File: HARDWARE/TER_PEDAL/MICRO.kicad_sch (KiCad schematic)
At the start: 21 parts, among them SW1 RST, U1 STM32F103C8Tx, Y1 8mHz

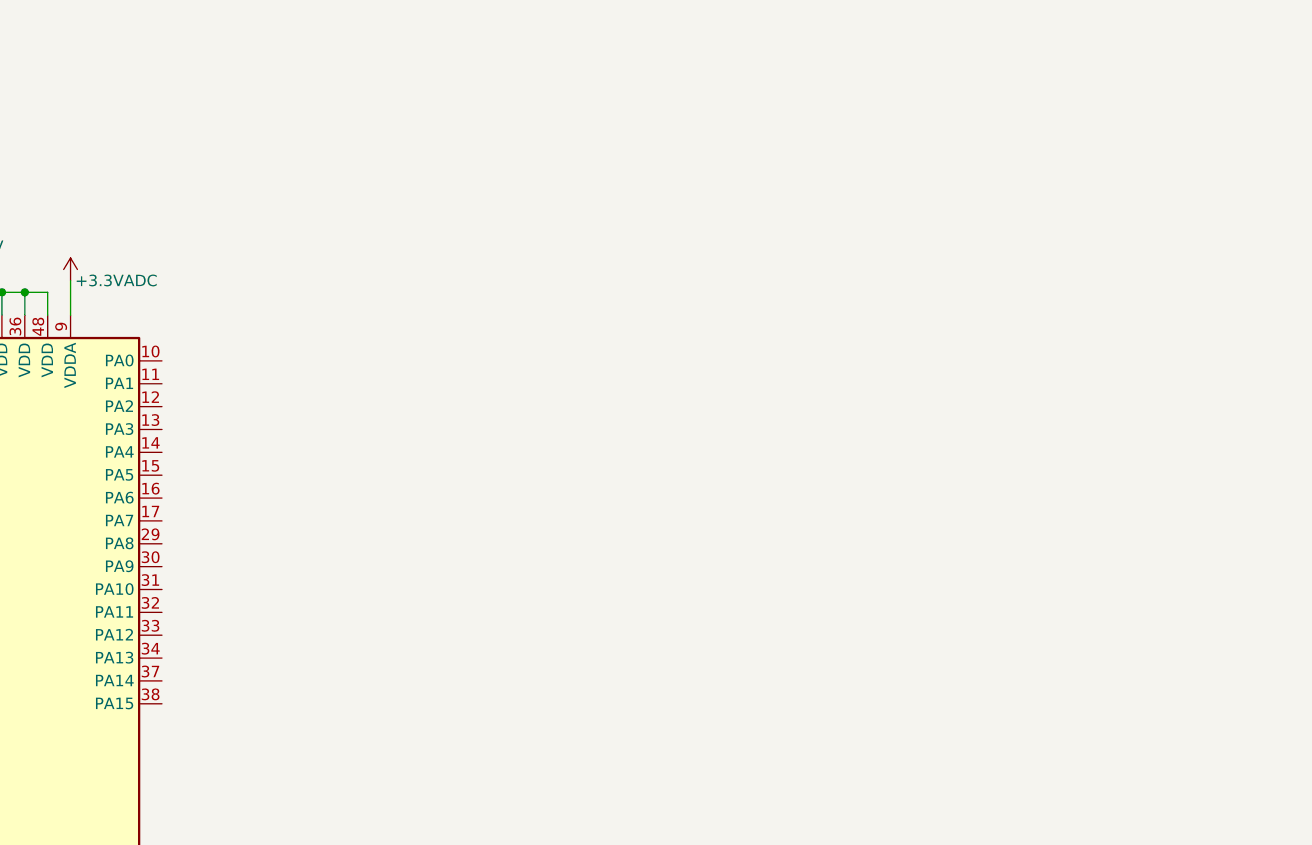
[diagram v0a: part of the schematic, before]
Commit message: Added Uniport, Debug and began sensors design
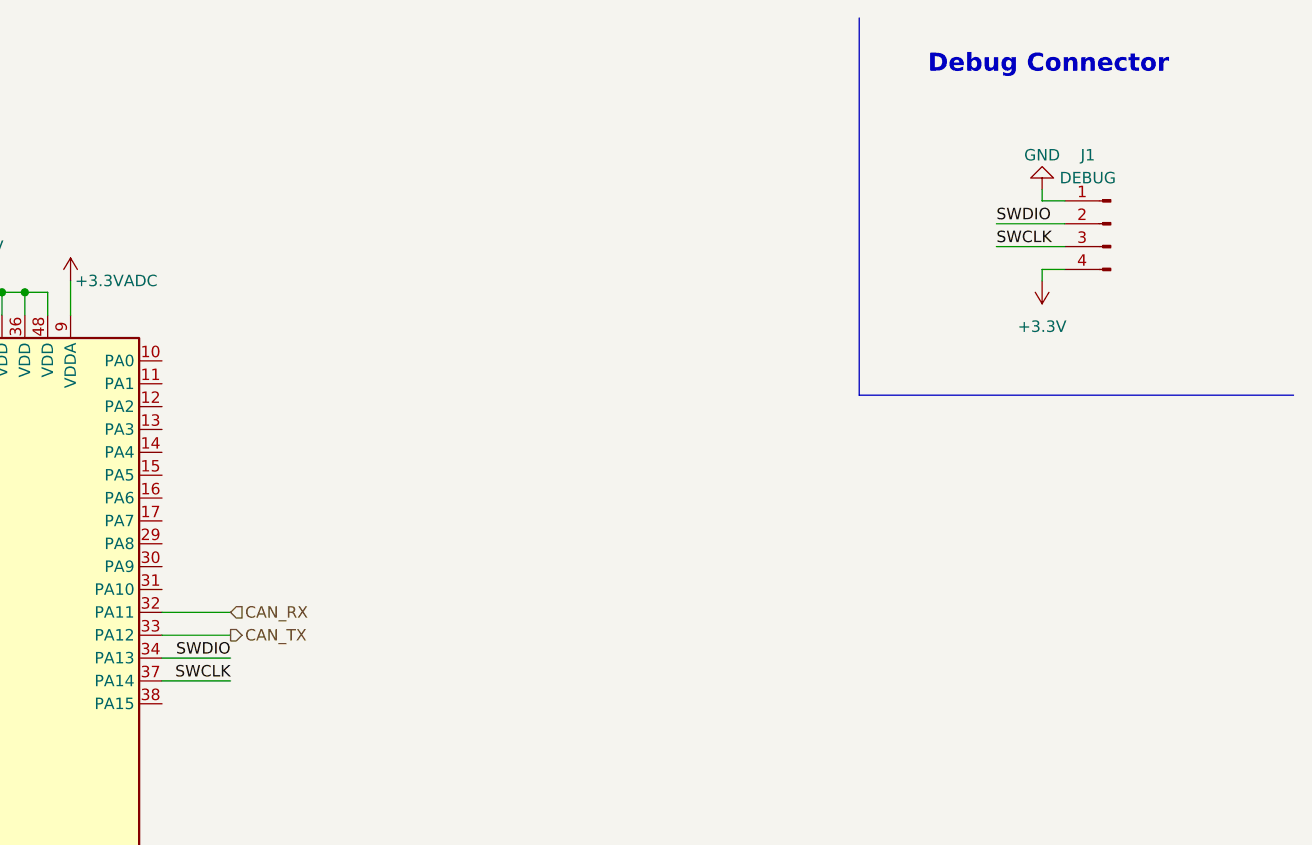
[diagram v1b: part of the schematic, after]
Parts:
- added J1: DEBUG, symbol Connector:Conn_01x04_Male
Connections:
- net GND: now also J1.1 (Pin_1)
- net CAN_RX: now reaches U1.32 (PA11)
- net CAN_TX: now reaches U1.33 (PA12)
- net SWDIO: now reaches U1.34 (PA13)
- net SWDIO: now also J1.2 (Pin_2)
- net SWCLK: now reaches U1.37 (PA14)
- net SWCLK: now also J1.3 (Pin_3)
- new net +3V3: J1.4 (Pin_4)
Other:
- note added: "Debug Connector"
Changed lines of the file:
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@@
+    (stroke (width 0) (type default))
+  )
+  (wire (pts (xy 158.75 83.82) (xy 166.37 83.82))
+    (stroke (width 0) (type default))
+  )
+  (wire (pts (xy 256.54 40.64) (xy 256.54 41.91))
     (stroke (width 0) (type default))
   )
@@
     (stroke (width 0) (type default))
   )
+  (wire (pts (xy 251.46 35.56) (xy 259.08 35.56))
+    (stroke (width 0) (type default))
+  )
   (wire (pts (xy 36.83 157.48) (xy 38.1 157.48))
     (stroke (width 0) (type default))
@@
     (stroke (width 0) (type default))
   )
+  (wire (pts (xy 256.54 31.75) (xy 256.54 33.02))
+    (stroke (width 0) (type default))
+  )
   (wire (pts (xy 138.43 41.91) (xy 138.43 43.18))
     (stroke (width 0) (type default))
@@
     (stroke (width 0) (type default))
   )
+  (wire (pts (xy 251.46 38.1) (xy 259.08 38.1))
+    (stroke (width 0) (type default))
+  )
   (wire (pts (xy 118.11 83.82) (xy 125.73 83.82))
     (stroke (width 0) (type default))
@@
     (stroke (width 0) (type default))
   )
+  (wire (pts (xy 158.75 86.36) (xy 166.37 86.36))
+    (stroke (width 0) (type default))
+  )
   (wire (pts (xy 148.59 41.91) (xy 148.59 45.72))
     (stroke (width 0) (type default))
@@
     (stroke (width 0) (type default))
   )
+  (polyline (pts (xy 236.22 54.61) (xy 284.48 54.61))
+    (stroke (width 0) (type default))
+  )
+  (polyline (pts (xy 236.22 12.7) (xy 236.22 54.61))
+    (stroke (width 0) (type default))
+  )
   (wire (pts (xy 143.51 43.18) (xy 146.05 43.18))
     (stroke (width 0) (type default))
@@
     (stroke (width 0) (type default))
   )
+  (wire (pts (xy 256.54 33.02) (xy 259.08 33.02))
+    (stroke (width 0) (type default))
+  )
   (wire (pts (xy 36.83 154.94) (xy 36.83 157.48))
     (stroke (width 0) (type default))
@@
     (stroke (width 0) (type default))
   )
+  (wire (pts (xy 158.75 78.74) (xy 166.37 78.74))
+    (stroke (width 0) (type default))
+  )
+  (wire (pts (xy 158.75 81.28) (xy 166.37 81.28))
+    (stroke (width 0) (type default))
+  )
   (wire (pts (xy 40.64 115.57) (xy 40.64 116.84))
     (stroke (width 0) (type default))
@@
   )
   (wire (pts (xy 24.13 115.57) (xy 24.13 116.84))
+    (stroke (width 0) (type default))
+  )
+  (wire (pts (xy 259.08 40.64) (xy 256.54 40.64))
     (stroke (width 0) (type default))
   )
@@
     (effects (font (size 1.27 1.27)) (justify left bottom))
   )
+  (text "Debug Connector" (at 243.84 19.05 0)
+    (effects (font (size 2 2) (thickness 0.4) bold) (justify left bottom))
+  )
+  (label "SWCLK" (at 251.46 38.1 0) (fields_autoplaced)
+    (effects (font (size 1.27 1.27)) (justify left bottom))
+  )
+  (label "SWCLK" (at 166.37 86.36 180) (fields_autoplaced)
+    (effects (font (size 1.27 1.27)) (justify right bottom))
+  )
+  (label "SWDIO" (at 251.46 35.56 0) (fields_autoplaced)
+    (effects (font (size 1.27 1.27)) (justify left bottom))
+  )
   (label "BOOT1" (at 118.11 83.82 0) (fields_autoplaced)
     (effects (font (size 1.27 1.27)) (justify left bottom))
@@
     (effects (font (size 1.27 1.27)) (justify left bottom))
   )
+  (label "SWDIO" (at 166.37 83.82 180) (fields_autoplaced)
+    (effects (font (size 1.27 1.27)) (justify right bottom))
+  )
   (label "NRST" (at 118.11 50.8 0) (fields_autoplaced)
     (effects (font (size 1.27 1.27)) (justify left bottom))
@@
   (label "BOOT1" (at 48.26 125.73 180) (fields_autoplaced)
     (effects (font (size 1.27 1.27)) (justify right bottom))
+  )
+  (hierarchical_label "CAN_RX" (shape input) (at 166.37 78.74 0) (fields_autoplaced)
+    (effects (font (size 1.27 1.27)) (justify left))
+  )
+  (hierarchical_label "CAN_TX" (shape output) (at 166.37 81.28 0) (fields_autoplaced)
+    (effects (font (size 1.27 1.27)) (justify left))
   )
   (symbol (lib_id "Device:C") (at 16.51 55.88 0) (unit 1)
@@
         (path "/73ede3a3-6344-40fe-9207-10ff50d388ba/7632a94a-0691-4527-83e2-6d814eae7e64"
           (reference "C1") (unit 1)
+        )
+      )
+    )
+  )
+  (symbol (lib_id "Connector:Conn_01x04_Male") (at 264.16 35.56 0) (mirror y) (unit 1)
+    (in_bom yes) (on_board yes) (dnp no)
+    (property "Reference" "J1" (at 261.62 27.94 0)
+      (effects (font (size 1.27 1.27)))
+    )
+    (property "Value" "DEBUG" (at 261.62 30.48 0)
+      (effects (font (size 1.27 1.27)))
+    )
+    (property "Footprint" "" (at 264.16 35.56 0)
+      (effects (font (size 1.27 1.27)) hide)
+    )
+    (property "Datasheet" "~" (at 264.16 35.56 0)
+      (effects (font (size 1.27 1.27)) hide)
+    )
+    (pin "1")
+    (pin "2")
+    (pin "3")
+    (pin "4")
+    (instances
+      (project "TER_PEDAL"
+        (path "/73ede3a3-6344-40fe-9207-10ff50d388ba/7632a94a-0691-4527-83e2-6d814eae7e64"
+          (reference "J1") (unit 1)
         )
       )
@@
     )
   )
+  (symbol (lib_name "GND_1") (lib_id "power:GND") (at 256.54 31.75 180) (unit 1)
+    (in_bom yes) (on_board yes) (dnp no) (fields_autoplaced)
+    (property "Reference" "#PWR032" (at 256.54 25.4 0)
+      (effects (font (size 1.27 1.27)) hide)
+    )
+    (property "Value" "GND" (at 256.54 27.94 0)
+      (effects (font (size 1.27 1.27)))
+    )
+    (property "Footprint" "" (at 256.54 31.75 0)
+      (effects (font (size 1.27 1.27)) hide)
+    )
+    (property "Datasheet" "" (at 256.54 31.75 0)
+      (effects (font (size 1.27 1.27)) hide)
+    )
+    (pin "1")
+    (instances
+      (project "TER_PEDAL"
+        (path "/73ede3a3-6344-40fe-9207-10ff50d388ba/7632a94a-0691-4527-83e2-6d814eae7e64"
+          (reference "#PWR032") (unit 1)
+        )
+      )
+    )
+  )
   (symbol (lib_id "Device:C_Small") (at 22.86 27.94 0) (unit 1)
     (in_bom yes) (on_board yes) (dnp no)
@@
         )
       )
+    )
+  )
+  (symbol (lib_name "+3.3V_1") (lib_id "power:+3.3V") (at 256.54 41.91 180) (unit 1)
+    (in_bom yes) (on_board yes) (dnp no) (fields_autoplaced)
+    (property "Reference" "#PWR033" (at 256.54 38.1 0)
+      (effects (font (size 1.27 1.27)) hide)
+    )
+    (property "Value" "+3.3V" (at 256.54 46.99 0)
+      (effects (font (size 1.27 1.27)))
+    )
+    (property "Footprint" "" (at 256.54 41.91 0)
+      (effects (font (size 1.27 1.27)) hide)
+    )
+    (property "Datasheet" "" (at 256.54 41.91 0)
+      (effects (font (size 1.27 1.27)) hide)
+    )
+    (pin "1")
+    (instances
+      (project "TER_PEDAL"
+        (path "/73ede3a3-6344-40fe-9207-10ff50d388ba/7632a94a-0691-4527-83e2-6d814eae7e64"
+          (reference "#PWR033") (unit 1)
+        )
+      )

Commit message: Added footprints to existing components
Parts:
- C1, C14, C15, C16, C2, C3, C4, C5: footprint (none) -> Capacitor_SMD:C_0603_1608Metric
- FB1: footprint Inductor_SMD:L_0805_2012Metric_Pad1.15x1.40mm_HandSolder -> Inductor_SMD:L_0603_1608Metric
- J1: footprint (none) -> Connector_PinHeader_2.00mm:PinHeader_1x04_P2.00mm_Vertical
- JP1, JP2: footprint (none) -> Connector_PinHeader_2.00mm:PinHeader_1x03_P2.00mm_Vertical
- R4, R5, R6, R7: footprint (none) -> Resistor_SMD:R_0603_1608Metric
- Y1: footprint (none) -> Crystal:Crystal_HC49-U_Vertical
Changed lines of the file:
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@@
       (effects (font (size 1.27 1.27)))
     )
-    (property "Footprint" "" (at 27.94 78.74 0)
+    (property "Footprint" "Resistor_SMD:R_0603_1608Metric" (at 27.94 78.74 0)
       (effects (font (size 1.27 1.27)) hide)
     )
@@
       (effects (font (size 1.27 1.27)) (justify left))
     )
-    (property "Footprint" "" (at 15.24 27.94 0)
+    (property "Footprint" "Capacitor_SMD:C_0603_1608Metric" (at 15.24 27.94 0)
       (effects (font (size 1.27 1.27)) hide)
     )
@@
       (effects (font (size 1.27 1.27)))
     )
-    (property "Footprint" "" (at 264.16 35.56 0)
+    (property "Footprint" "Connector_PinHeader_2.00mm:PinHeader_1x04_P2.00mm_Vertical" (at 264.16 35.56 0)
       (effects (font (size 1.27 1.27)) hide)
     )
@@
       (effects (font (size 1.27 1.27)) (justify left))
     )
-    (property "Footprint" "" (at 40.64 119.38 0)
+    (property "Footprint" "Resistor_SMD:R_0603_1608Metric" (at 40.64 119.38 0)
       (effects (font (size 1.27 1.27)) hide)
     )
@@
       (effects (font (size 1.27 1.27)) (justify left))
     )
-    (property "Footprint" "" (at 38.1 27.94 0)
+    (property "Footprint" "Capacitor_SMD:C_0603_1608Metric" (at 38.1 27.94 0)
       (effects (font (size 1.27 1.27)) hide)
     )
@@
       (effects (font (size 1.27 1.27)))
     )
-    (property "Footprint" "" (at 40.64 111.76 0)
+    (property "Footprint" "Connector_PinHeader_2.00mm:PinHeader_1x03_P2.00mm_Vertical" (at 40.64 111.76 0)
       (effects (font (size 1.27 1.27)) hide)
     )
@@
       (effects (font (size 1.27 1.27)))
     )
-    (property "Footprint" "" (at 25.4 156.5148 0)
+    (property "Footprint" "Capacitor_SMD:C_0603_1608Metric" (at 25.4 156.5148 0)
       (effects (font (size 1.27 1.27)) hide)
     )
@@
       (effects (font (size 1.27 1.27)))
     )
-    (property "Footprint" "" (at 24.13 111.76 0)
+    (property "Footprint" "Connector_PinHeader_2.00mm:PinHeader_1x03_P2.00mm_Vertical" (at 24.13 111.76 0)
       (effects (font (size 1.27 1.27)) hide)
     )
@@
       (effects (font (size 1.27 1.27)) (justify left))
     )
-    (property "Footprint" "" (at 45.72 27.94 0)
+    (property "Footprint" "Capacitor_SMD:C_0603_1608Metric" (at 45.72 27.94 0)
       (effects (font (size 1.27 1.27)) hide)
     )
@@
       (effects (font (size 1.27 1.27)))
     )
-    (property "Footprint" "" (at 31.75 157.48 0)
+    (property "Footprint" "Crystal:Crystal_HC49-U_Vertical" (at 31.75 157.48 0)
       (effects (font (size 1.27 1.27)) hide)
     )
@@
       (effects (font (size 1.27 1.27)) (justify left))
     )
-    (property "Footprint" "" (at 35.052 151.13 90)
+    (property "Footprint" "Resistor_SMD:R_0603_1608Metric" (at 35.052 151.13 90)
       (effects (font (size 1.27 1.27)) hide)
     )
@@
       (effects (font (size 1.27 1.27)) (justify left))
     )
-    (property "Footprint" "" (at 22.86 27.94 0)
+    (property "Footprint" "Capacitor_SMD:C_0603_1608Metric" (at 22.86 27.94 0)
       (effects (font (size 1.27 1.27)) hide)
     )
@@
       (effects (font (size 1.27 1.27)) (justify left))
     )
-    (property "Footprint" "" (at 30.48 27.94 0)
+    (property "Footprint" "Capacitor_SMD:C_0603_1608Metric" (at 30.48 27.94 0)
       (effects (font (size 1.27 1.27)) hide)
     )
@@
       (effects (font (size 1.27 1.27)) (justify left))
     )
-    (property "Footprint" "" (at 33.9852 88.9 0)
+    (property "Footprint" "Capacitor_SMD:C_0603_1608Metric" (at 33.9852 88.9 0)
       (effects (font (size 1.27 1.27)) hide)
     )
@@
       (effects (font (size 1.27 1.27)) (justify left))
     )
-    (property "Footprint" "" (at 24.13 119.38 0)
+    (property "Footprint" "Resistor_SMD:R_0603_1608Metric" (at 24.13 119.38 0)
       (effects (font (size 1.27 1.27)) hide)
     )
@@
       (effects (font (size 1.27 1.27)))
     )
-    (property "Footprint" "Inductor_SMD:L_0805_2012Metric_Pad1.15x1.40mm_HandSolder" (at 35.56 52.578 90)
+    (property "Footprint" "Inductor_SMD:L_0603_1608Metric" (at 35.56 52.578 90)
       (effects (font (size 1.27 1.27)) hide)
     )
@@
       (effects (font (size 1.27 1.27)))
     )
-    (property "Footprint" "" (at 45.72 156.5148 0)
-      (effects (font (size 1.27 1.27)) hide)
-    )
+    (property "Footprint" "Capacitor_SMD:C_0603_1608Metric" (at 45.72 156.5148 0)
+      (effects (font (size 1.27 1.27)) hide)
+    )

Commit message: Finished Initial Schematic
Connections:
- net APPS_1_ADC: now reaches U1.10 (PA0)
- net APPS_2_ADC: now reaches U1.11 (PA1)
- net BPPS_ADC: now reaches U1.12 (PA2)
- net IMP_LED: now reaches U1.39 (PB3)
- net DBG_LED: now reaches U1.40 (PB4)
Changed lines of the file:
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@@
+    (stroke (width 0) (type default))
+  )
+  (wire (pts (xy 160.02 55.88) (xy 158.75 55.88))
     (stroke (width 0) (type default))
   )
@@
     (stroke (width 0) (type default))
   )
+  (wire (pts (xy 160.02 53.34) (xy 158.75 53.34))
+    (stroke (width 0) (type default))
+  )
   (wire (pts (xy 256.54 33.02) (xy 259.08 33.02))
     (stroke (width 0) (type default))
@@
   )
   (polyline (pts (xy 52.07 128.27) (xy 52.07 198.12))
+    (stroke (width 0) (type default))
+  )
+  (wire (pts (xy 160.02 50.8) (xy 158.75 50.8))
     (stroke (width 0) (type default))
   )
@@
     (effects (font (size 1.27 1.27)) (justify right bottom))
   )
+  (hierarchical_label "DBG_LED" (shape input) (at 125.73 88.9 180) (fields_autoplaced)
+    (effects (font (size 1.27 1.27)) (justify right))
+  )
   (hierarchical_label "CAN_RX" (shape input) (at 166.37 78.74 0) (fields_autoplaced)
     (effects (font (size 1.27 1.27)) (justify left))
   )
+  (hierarchical_label "APPS_2_ADC" (shape input) (at 160.02 53.34 0) (fields_autoplaced)
+    (effects (font (size 1.27 1.27)) (justify left))
+  )
+  (hierarchical_label "APPS_1_ADC" (shape input) (at 160.02 50.8 0) (fields_autoplaced)
+    (effects (font (size 1.27 1.27)) (justify left))
+  )
+  (hierarchical_label "IMP_LED" (shape input) (at 125.73 86.36 180) (fields_autoplaced)
+    (effects (font (size 1.27 1.27)) (justify right))
+  )
+  (hierarchical_label "BPPS_ADC" (shape input) (at 160.02 55.88 0) (fields_autoplaced)
+    (effects (font (size 1.27 1.27)) (justify left))
+  )

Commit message: Started Layout and fixed wrong footprints
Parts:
- removed SW1: RST, Button_Switch_SMD:SW_MEC_5GSH9, symbol Switch:SW_MEC_5G
- added SW1: RST, Button_Switch_SMD:SW_SPST_EVQPE1, symbol Switch:SW_SPST
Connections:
- net GND: now also SW1.1 (A)
- net at R7.1: now also SW1.2 (B)
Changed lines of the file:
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@@
-    )
-  )
-  (symbol (lib_id "Switch:SW_MEC_5G") (at 22.86 85.09 90) (unit 1)
-    (in_bom yes) (on_board yes) (dnp no) (fields_autoplaced)
-    (property "Reference" "SW1" (at 24.13 84.455 90)
-      (effects (font (size 1.27 1.27)) (justify right))
-    )
-    (property "Value" "RST" (at 24.13 86.995 90)
-      (effects (font (size 1.27 1.27)) (justify right))
-    )
-    (property "Footprint" "Button_Switch_SMD:SW_MEC_5GSH9" (at 17.78 85.09 0)
-      (effects (font (size 1.27 1.27)) hide)
-    )
-    (property "Datasheet" "http://www.apem.com/int/index.php?controller=attachment&id_attachment=488" (at 17.78 85.09 0)
-      (effects (font (size 1.27 1.27)) hide)
-    )
-    (pin "1")
-    (pin "3")
-    (pin "2")
-    (pin "4")
-    (instances
-      (project "TER_PEDAL"
-        (path "/73ede3a3-6344-40fe-9207-10ff50d388ba/7632a94a-0691-4527-83e2-6d814eae7e64"
-          (reference "SW1") (unit 1)
-        )
-      )
     )
   )
@@
         )
       )
+    )
+  )
+  (symbol (lib_id "Switch:SW_SPST") (at 22.86 85.09 90) (unit 1)
+    (in_bom yes) (on_board yes) (dnp no) (fields_autoplaced)
+    (property "Reference" "SW1" (at 24.13 84.455 90)
+      (effects (font (size 1.27 1.27)) (justify right))
+    )
+    (property "Value" "RST" (at 24.13 86.995 90)
+      (effects (font (size 1.27 1.27)) (justify right))
+    )
+    (property "Footprint" "Button_Switch_SMD:SW_SPST_EVQPE1" (at 22.86 85.09 0)
+      (effects (font (size 1.27 1.27)) hide)
+    )
+    (property "Datasheet" "~" (at 22.86 85.09 0)
+      (effects (font (size 1.27 1.27)) hide)
+    )
+    (pin "1")
+    (pin "2")
+    (instances
+      (project "TER_PEDAL"
+        (path "/73ede3a3-6344-40fe-9207-10ff50d388ba/7632a94a-0691-4527-83e2-6d814eae7e64"
+          (reference "SW1") (unit 1)
+        )
+      )

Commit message: Sized and Fixed even more footprints + Initial layout
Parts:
- C1, C2, C3, C4: footprint Capacitor_SMD:C_0603_1608Metric -> Capacitor_SMD:C_0402_1005Metric
- FB1: footprint Inductor_SMD:L_0603_1608Metric -> Inductor_SMD:L_0402_1005Metric
- R6: footprint Resistor_SMD:R_0603_1608Metric -> Resistor_SMD:R_0402_1005Metric
- SW1: footprint Button_Switch_SMD:SW_SPST_EVQPE1 -> Button_Switch_SMD:SW_Tactile_SPST_NO_Straight_CK_PTS636Sx25SMTRLFS
- Y1: footprint Crystal:Crystal_HC49-U_Vertical -> Crystal:Crystal_HC52-6mm_Vertical
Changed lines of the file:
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@@
       (effects (font (size 1.27 1.27)) (justify left))
     )
-    (property "Footprint" "Capacitor_SMD:C_0603_1608Metric" (at 38.1 27.94 0)
+    (property "Footprint" "Capacitor_SMD:C_0402_1005Metric" (at 38.1 27.94 0)
       (effects (font (size 1.27 1.27)) hide)
     )
@@
       (effects (font (size 1.27 1.27)) (justify left))
     )
-    (property "Footprint" "Capacitor_SMD:C_0603_1608Metric" (at 45.72 27.94 0)
+    (property "Footprint" "Capacitor_SMD:C_0402_1005Metric" (at 45.72 27.94 0)
       (effects (font (size 1.27 1.27)) hide)
     )
@@
       (effects (font (size 1.27 1.27)))
     )
-    (property "Footprint" "Crystal:Crystal_HC49-U_Vertical" (at 31.75 157.48 0)
+    (property "Footprint" "Crystal:Crystal_HC52-6mm_Vertical" (at 31.75 157.48 0)
       (effects (font (size 1.27 1.27)) hide)
     )
@@
       (effects (font (size 1.27 1.27)) (justify left))
     )
-    (property "Footprint" "Resistor_SMD:R_0603_1608Metric" (at 35.052 151.13 90)
+    (property "Footprint" "Resistor_SMD:R_0402_1005Metric" (at 35.052 151.13 90)
       (effects (font (size 1.27 1.27)) hide)
     )
@@
       (effects (font (size 1.27 1.27)) (justify left))
     )
-    (property "Footprint" "Capacitor_SMD:C_0603_1608Metric" (at 22.86 27.94 0)
+    (property "Footprint" "Capacitor_SMD:C_0402_1005Metric" (at 22.86 27.94 0)
       (effects (font (size 1.27 1.27)) hide)
     )
@@
       (effects (font (size 1.27 1.27)) (justify left))
     )
-    (property "Footprint" "Capacitor_SMD:C_0603_1608Metric" (at 30.48 27.94 0)
+    (property "Footprint" "Capacitor_SMD:C_0402_1005Metric" (at 30.48 27.94 0)
       (effects (font (size 1.27 1.27)) hide)
     )
@@
       (effects (font (size 1.27 1.27)) (justify right))
     )
-    (property "Footprint" "Button_Switch_SMD:SW_SPST_EVQPE1" (at 22.86 85.09 0)
+    (property "Footprint" "Button_Switch_SMD:SW_Tactile_SPST_NO_Straight_CK_PTS636Sx25SMTRLFS" (at 22.86 85.09 0)
       (effects (font (size 1.27 1.27)) hide)
     )
@@
       (effects (font (size 1.27 1.27)))
     )
-    (property "Footprint" "Inductor_SMD:L_0603_1608Metric" (at 35.56 52.578 90)
-      (effects (font (size 1.27 1.27)) hide)
-    )
+    (property "Footprint" "Inductor_SMD:L_0402_1005Metric" (at 35.56 52.578 90)
+      (effects (font (size 1.27 1.27)) hide)
+    )
